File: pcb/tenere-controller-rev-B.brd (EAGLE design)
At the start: 64 x 99 mm, 45 parts, among them U1 BLUEPILL, U4 LD1117S33TR, U5 WIN850IO

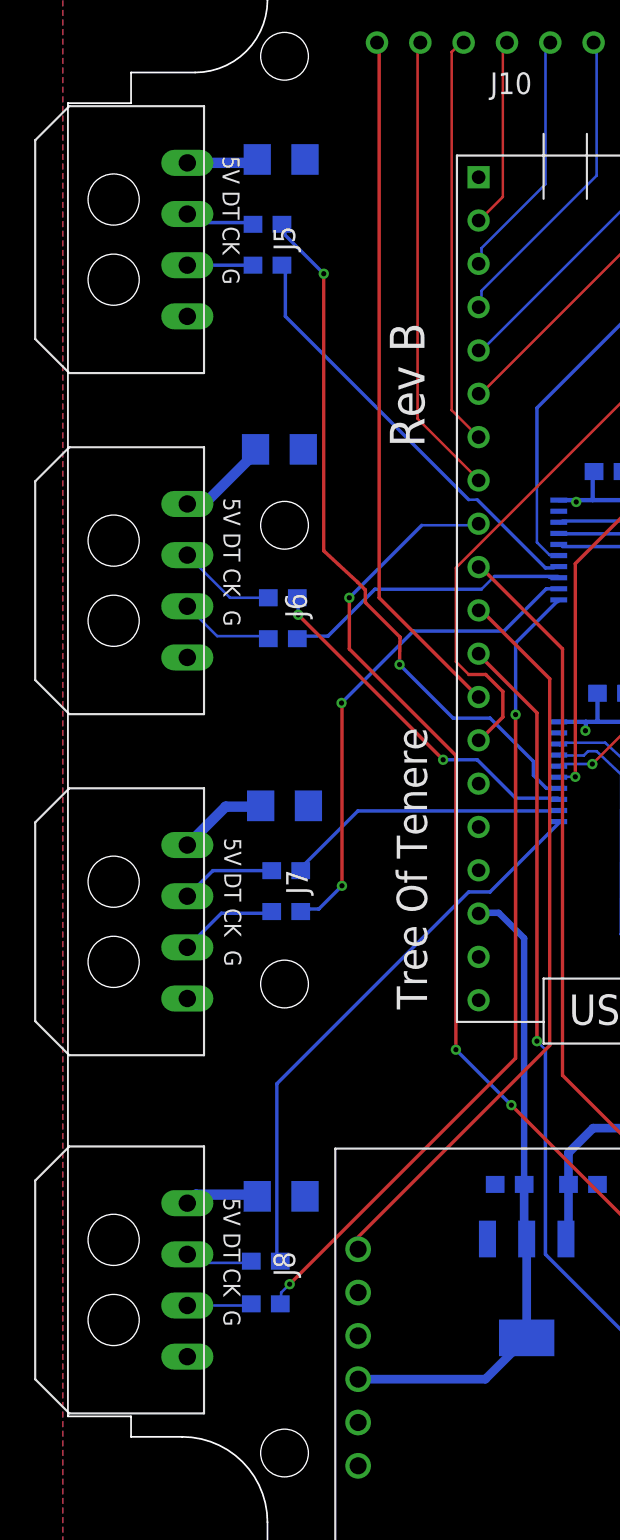
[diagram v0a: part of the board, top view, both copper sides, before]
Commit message: Minor change to one of the connectors
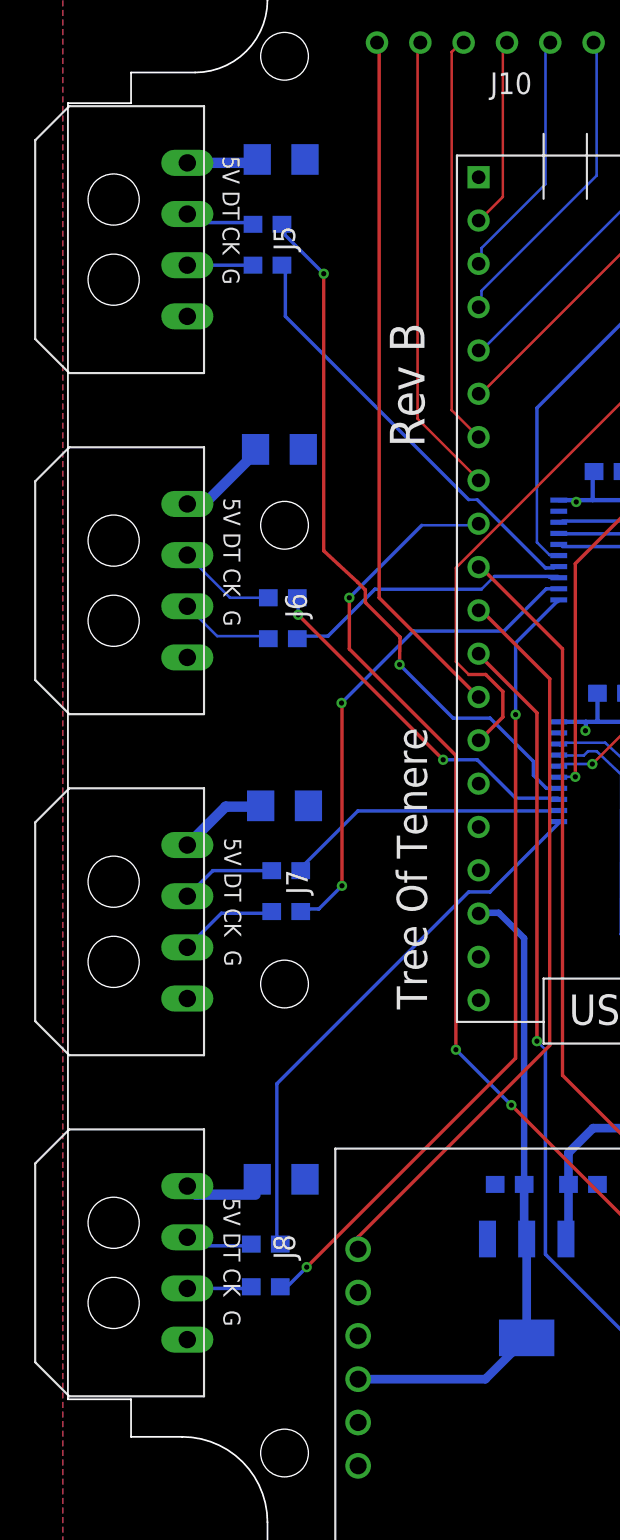
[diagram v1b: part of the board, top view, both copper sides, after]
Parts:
- moved C8 1.00 mm to (13.5, 27.9)
- moved J8 1.00 mm to (8.00, 23.0)
- moved R15 1.00 mm to (12.6, 24.1)
- moved R16 1.00 mm to (12.6, 21.6)
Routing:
- net CLKOUT8: track 33.7 -> 32.7 mm
- net VIN: track 76.4 -> 77.1 mm
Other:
- outline, holes or cut-outs redrawn
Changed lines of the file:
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@@
 <grid distance="0.001" unitdist="inch" unit="inch" style="lines" multiple="1" display="yes" altdistance="0.01" altunitdist="inch" altunit="inch"/>
 <layers>
-<layer number="1" name="Top" color="4" fill="1" visible="no" active="yes"/>
+<layer number="1" name="Top" color="4" fill="1" visible="yes" active="yes"/>
 <layer number="2" name="Route2" color="1" fill="3" visible="no" active="no"/>
 <layer number="3" name="Route3" color="4" fill="3" visible="no" active="no"/>
@@
 <layer number="19" name="Unrouted" color="6" fill="1" visible="yes" active="yes"/>
 <layer number="20" name="Dimension" color="15" fill="1" visible="yes" active="yes"/>
-<layer number="21" name="tPlace" color="7" fill="1" visible="no" active="yes"/>
+<layer number="21" name="tPlace" color="7" fill="1" visible="yes" active="yes"/>
 <layer number="22" name="bPlace" color="7" fill="1" visible="yes" active="yes"/>
 <layer number="23" name="tOrigins" color="15" fill="1" visible="yes" active="yes"/>
@@
 <wire x1="12.7" y1="7.8" x2="7.7" y2="12.8" width="0.1" layer="20" curve="90"/>
 <wire x1="7.7" y1="12.8" x2="4.7" y2="12.8" width="0.1" layer="20"/>
-<wire x1="4.7" y1="12.8" x2="4.7" y2="14" width="0.1" layer="20"/>
-<wire x1="4.7" y1="14" x2="1" y2="14" width="0.1" layer="20"/>
-<wire x1="1" y1="14" x2="1" y2="91" width="0.1" layer="20"/>
+<wire x1="4.7" y1="12.8" x2="4.7" y2="15" width="0.1" layer="20"/>
+<wire x1="4.7" y1="15" x2="1" y2="15" width="0.1" layer="20"/>
+<wire x1="1" y1="15" x2="1" y2="91" width="0.1" layer="20"/>
 <wire x1="1" y1="91" x2="4.7" y2="91" width="0.1" layer="20"/>
 <wire x1="4.7" y1="91" x2="4.7" y2="92.8" width="0.1" layer="20"/>
@@
 <attribute name="NAME" x="11.16" y="49.673" size="0.8128" layer="26" ratio="18" rot="MR0"/>
 </element>
-<element name="R15" library="microbuilder" package="0603" value="" x="12.6" y="23.1" smashed="yes" rot="MR0">
-<attribute name="NAME" x="10.822" y="22.973" size="0.8128" layer="26" font="vector" ratio="18" rot="MR0"/>
-<attribute name="VALUE" x="10.822" y="22.338" size="0.4064" layer="28" font="vector" ratio="10" rot="MR0"/>
-</element>
-<element name="R16" library="microbuilder" package="0603" value="" x="12.6" y="20.6" smashed="yes" rot="MR0">
-<attribute name="NAME" x="10.822" y="20.473" size="0.8128" layer="26" font="vector" ratio="18" rot="MR0"/>
-<attribute name="VALUE" x="10.822" y="19.838" size="0.4064" layer="28" font="vector" ratio="10" rot="MR0"/>
-</element>
-<element name="C8" library="microbuilder" package="1206" value="100uF" x="13.5" y="26.9" smashed="yes" rot="MR0">
-<attribute name="NAME" x="10.96" y="26.773" size="0.8128" layer="26" ratio="18" rot="MR0"/>
+<element name="R15" library="microbuilder" package="0603" value="" x="12.6" y="24.1" smashed="yes" rot="MR0">
+<attribute name="NAME" x="10.822" y="23.973" size="0.8128" layer="26" font="vector" ratio="18" rot="MR0"/>
+<attribute name="VALUE" x="10.822" y="23.338" size="0.4064" layer="28" font="vector" ratio="10" rot="MR0"/>
+</element>
+<element name="R16" library="microbuilder" package="0603" value="" x="12.6" y="21.6" smashed="yes" rot="MR0">
+<attribute name="NAME" x="10.822" y="21.473" size="0.8128" layer="26" font="vector" ratio="18" rot="MR0"/>
+<attribute name="VALUE" x="10.822" y="20.838" size="0.4064" layer="28" font="vector" ratio="10" rot="MR0"/>
+</element>
+<element name="C8" library="microbuilder" package="1206" value="100uF" x="13.5" y="27.9" smashed="yes" rot="MR0">
+<attribute name="NAME" x="10.96" y="27.773" size="0.8128" layer="26" ratio="18" rot="MR0"/>
 </element>
 <element name="C11" library="microbuilder" package="0603" value="0.1uF" x="32.7" y="69.4" smashed="yes" rot="MR0">
@@
 <attribute name="NAME" x="15.0612" y="44.6002" size="1.27" layer="25" rot="R90"/>
 </element>
-<element name="J8" library="Custom" package="43650-0400" value="" x="8" y="22" smashed="yes" rot="R90">
-<attribute name="NAME" x="14.3246" y="22.2032" size="1.27" layer="25" rot="R90"/>
+<element name="J8" library="Custom" package="43650-0400" value="" x="8" y="23" smashed="yes" rot="R90">
+<attribute name="NAME" x="14.3246" y="23.2032" size="1.27" layer="25" rot="R90"/>
 </element>
 <element name="SW1" library="Custom" package="1825027" value="" x="44.3412" y="98.5866" rot="R180"/>
@@
 <wire x1="29.25" y1="35.75" x2="29.25" y2="57.25" width="0.2032" layer="1"/>
 <wire x1="18" y1="24.5" x2="29.25" y2="35.75" width="0.2032" layer="1"/>
-<wire x1="18" y1="24" x2="18" y2="24.5" width="0.1524" layer="1"/>
+<wire x1="18" y1="24" x2="18" y2="24.5" width="0.2032" layer="1"/>
 <wire x1="25.25" y1="61.25" x2="25.08" y2="61.26" width="0.1524" layer="1"/>
 <wire x1="18" y1="24" x2="18.0162" y2="23.8" width="0.1524" layer="1"/>
@@
 <wire x1="31.369" y1="54.2036" x2="31.369" y2="54.725" width="0.254" layer="16"/>
 <wire x1="8.5" y1="27" x2="12" y2="27" width="0.6096" layer="16"/>
-<wire x1="8" y1="26.5" x2="8.5" y2="27" width="0.6096" layer="16"/>
-<wire x1="12" y1="27" x2="12.1" y2="26.9" width="0.1524" layer="16"/>
+<wire x1="8" y1="27.5" x2="8.5" y2="27" width="0.6096" layer="16"/>
+<wire x1="12" y1="27" x2="12.1" y2="27.9" width="0.1524" layer="16"/>
 <wire x1="10.25" y1="49.75" x2="12.25" y2="49.75" width="0.6096" layer="16"/>
 <wire x1="8" y1="47.5" x2="10.25" y2="49.75" width="0.6096" layer="16"/>
@@
 <contactref element="R15" pad="2"/>
 <contactref element="J8" pad="3"/>
-<wire x1="8.5" y1="23" x2="11.75" y2="23" width="0.1524" layer="16"/>
-<wire x1="8" y1="23.5" x2="8.5" y2="23" width="0.1524" layer="16"/>
-<wire x1="11.75" y1="23" x2="11.75" y2="23.1" width="0.1524" layer="16"/>
+<wire x1="8.5" y1="24" x2="11.75" y2="24" width="0.2032" layer="16"/>
+<wire x1="8" y1="24.5" x2="8.5" y2="24" width="0.2032" layer="16"/>
+<wire x1="11.75" y1="24" x2="11.75" y2="24.1" width="0.1524" layer="16"/>
 </signal>
 <signal name="N$20">
 <contactref element="R16" pad="2"/>
 <contactref element="J8" pad="2"/>
-<wire x1="8" y1="20.5" x2="11.75" y2="20.5" width="0.1524" layer="16"/>
-<wire x1="11.75" y1="20.5" x2="11.75" y2="20.6" width="0.1524" layer="16"/>
+<wire x1="8" y1="21.5" x2="11.75" y2="21.5" width="0.2032" layer="16"/>
+<wire x1="11.75" y1="21.5" x2="11.75" y2="21.6" width="0.1524" layer="16"/>
 </signal>
 <signal name="DATAOUT2">
@@
 <contactref element="R16" pad="1"/>
 <wire x1="27.25" y1="35" x2="27.25" y2="55.147" width="0.2032" layer="1"/>
-<wire x1="14" y1="21.75" x2="27.25" y2="35" width="0.2032" layer="1"/>
-<wire x1="13.5" y1="21.25" x2="14" y2="21.75" width="0.1524" layer="16"/>
-<wire x1="13.5" y1="20.75" x2="13.5" y2="21.25" width="0.1524" layer="16"/>
+<wire x1="15" y1="22.75" x2="27.25" y2="35" width="0.2032" layer="1"/>
+<wire x1="13.5" y1="21.25" x2="15" y2="22.75" width="0.2032" layer="16"/>
+<wire x1="13.5" y1="21.75" x2="13.5" y2="21.25" width="0.1524" layer="16"/>
 <wire x1="29.75" y1="61.75" x2="29.7822" y2="61.875" width="0.1524" layer="16"/>
-<wire x1="13.5" y1="20.75" x2="13.45" y2="20.6" width="0.1524" layer="16"/>
+<wire x1="13.5" y1="21.75" x2="13.45" y2="21.6" width="0.1524" layer="16"/>
 <via x="27.25" y="55.147" extent="1-16" drill="0.3048"/>
-<via x="14" y="21.75" extent="1-16" drill="0.3048"/>
+<via x="15" y="22.75" extent="1-16" drill="0.3048"/>
 <wire x1="27.25" y1="55.147" x2="27.25" y2="59.3428" width="0.2032" layer="16"/>
 <wire x1="27.25" y1="59.3428" x2="29.7822" y2="61.875" width="0.2032" layer="16"/>
@@
 <wire x1="24.5" y1="44.75" x2="25.75" y2="44.75" width="0.2032" layer="16"/>
 <wire x1="13.25" y1="33.5" x2="24.5" y2="44.75" width="0.2032" layer="16"/>
-<wire x1="13.25" y1="23.25" x2="13.25" y2="33.5" width="0.2032" layer="16"/>
+<wire x1="13.25" y1="24.25" x2="13.25" y2="33.5" width="0.2032" layer="16"/>
 <wire x1="29.75" y1="48.75" x2="29.7822" y2="48.875" width="0.1524" layer="16"/>
-<wire x1="13.25" y1="23.25" x2="13.45" y2="23.1" width="0.1524" layer="16"/>
+<wire x1="13.25" y1="24.25" x2="13.45" y2="24.1" width="0.1524" layer="16"/>
 </signal>
 <signal name="DATA1">
